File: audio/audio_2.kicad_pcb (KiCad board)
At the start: 2 copper layers, 15.2 x 54.6 mm, 2 parts, among them J1 Comum, J2 RPI

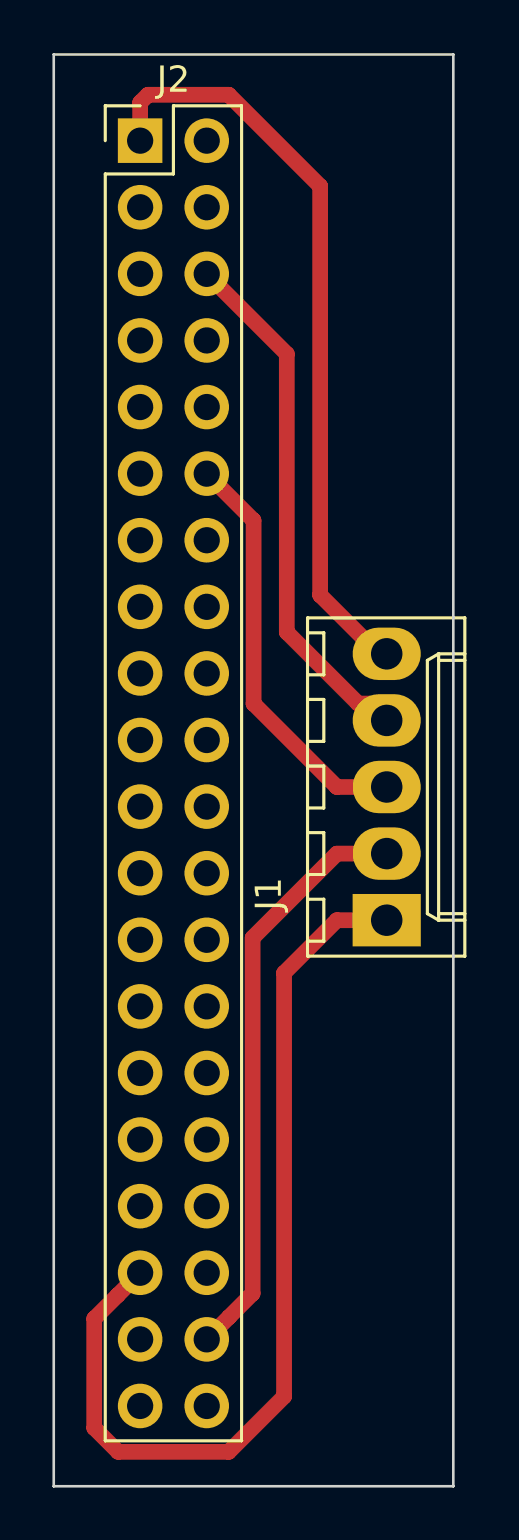
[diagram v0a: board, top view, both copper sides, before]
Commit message: Corrigida alimentação do led, botão e resistor de pull down
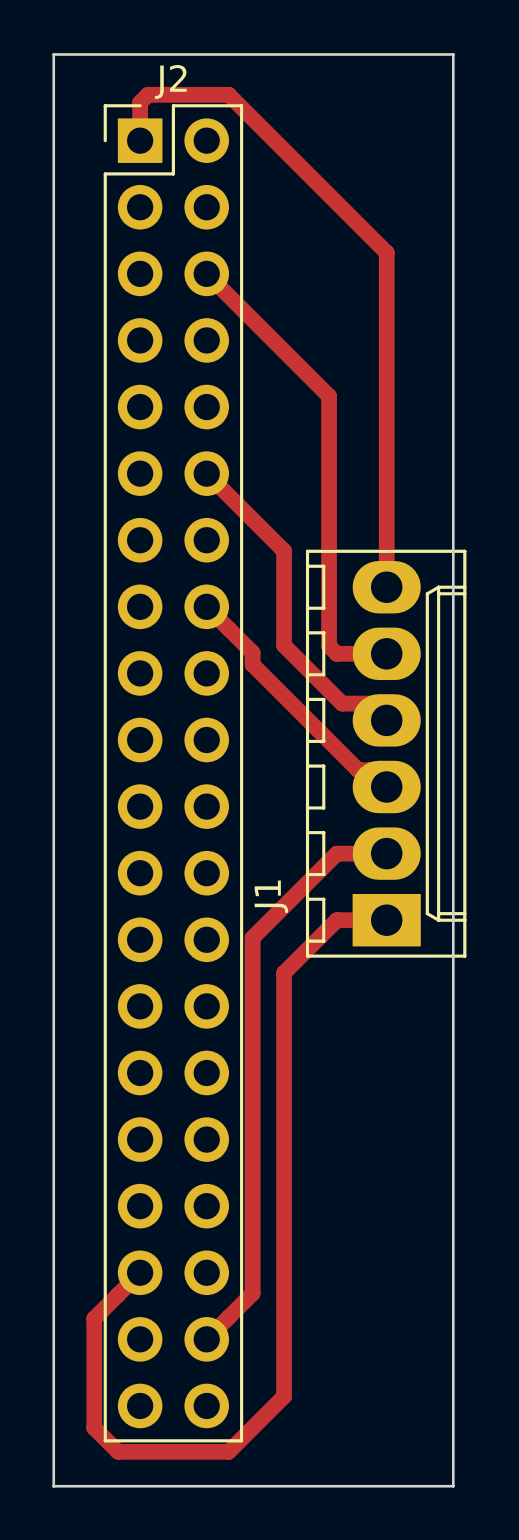
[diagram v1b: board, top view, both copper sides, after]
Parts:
- J1: value Comum -> Conn_01x06; footprint Connectors_Molex:Molex_KK-6410-05_05x2.54mm_Straight -> Connectors_Molex:Molex_KK-6410-06_06x2.54mm_Straight
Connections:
- J1 pad 3: bclk -> Net-(J1-Pad3)
- J1 pad 4: gnd -> bclk
- J1 pad 5: 3.3v -> gnd
- J2 pad 16: Net-(J2-Pad16) -> Net-(J1-Pad3)
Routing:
- net Net-(J1-Pad3): track 0.00 -> 9.98 mm
- net bclk: track 15.9 -> 12.9 mm
- net 3.3v: track 28.9 -> 26.2 mm
- net gnd: track 20.1 -> 18.4 mm
- removed copper zone on F.Cu, net (none)
